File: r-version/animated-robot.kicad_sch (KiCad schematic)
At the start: 4 parts, among them J1 USB_C_Receptacle_USB2.0_16P, J2 Conn_02x03_Odd_Even, U1 LKS32MC034DOFxQx

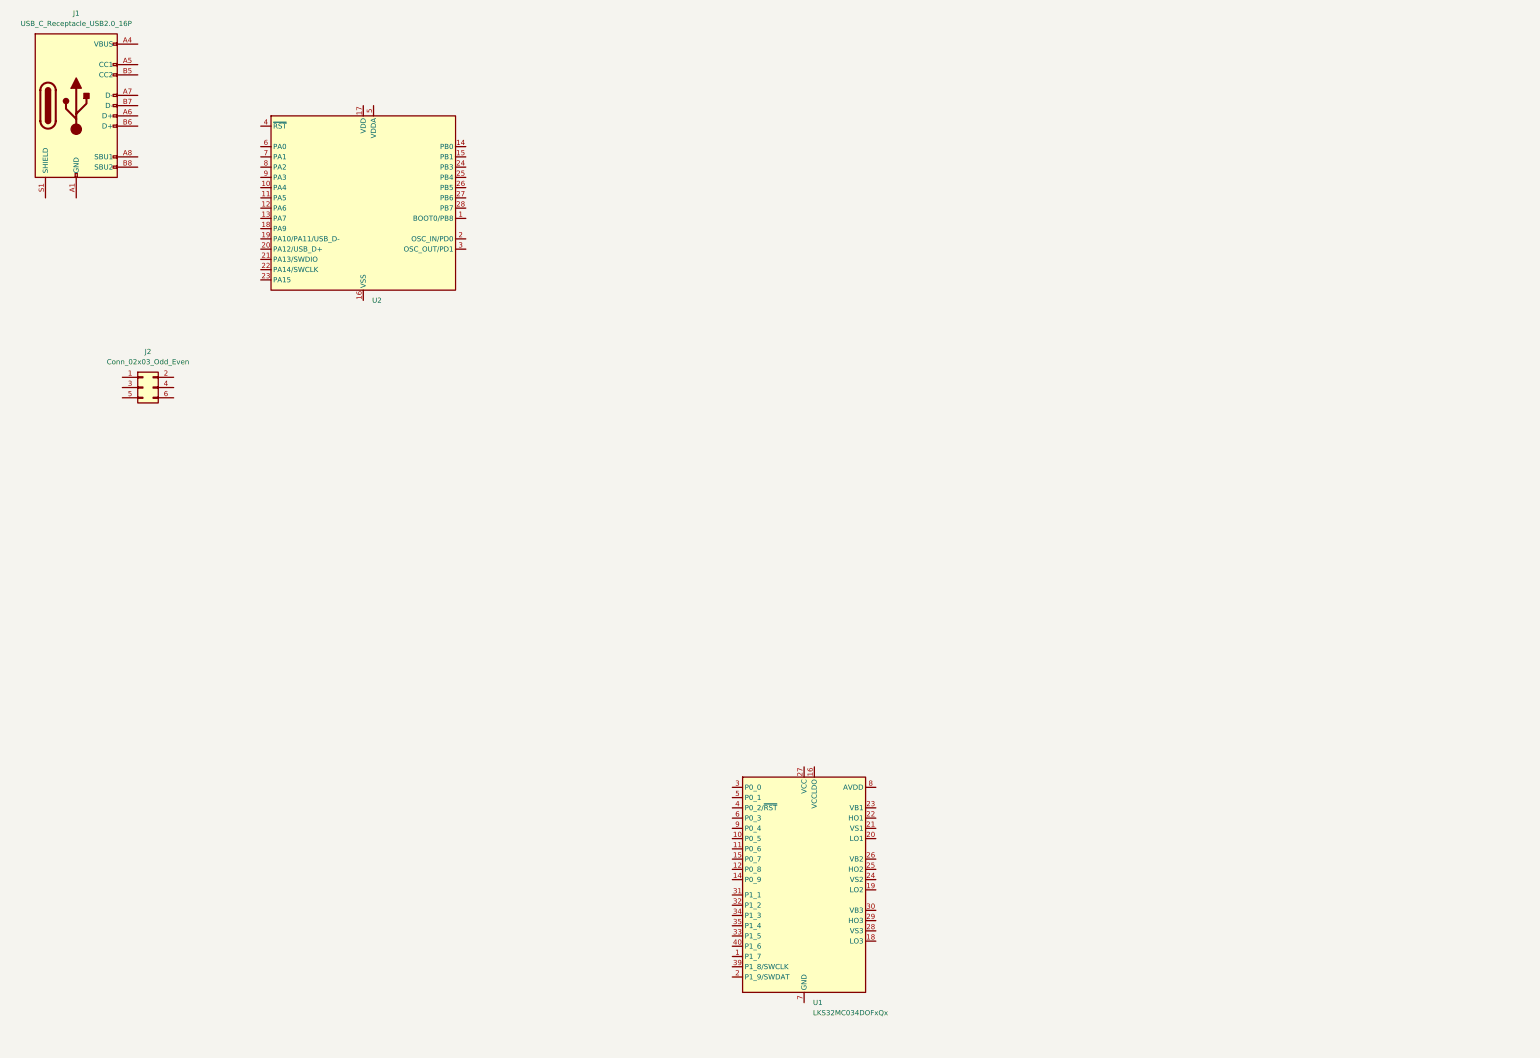
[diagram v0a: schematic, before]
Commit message: wch usb bridge section
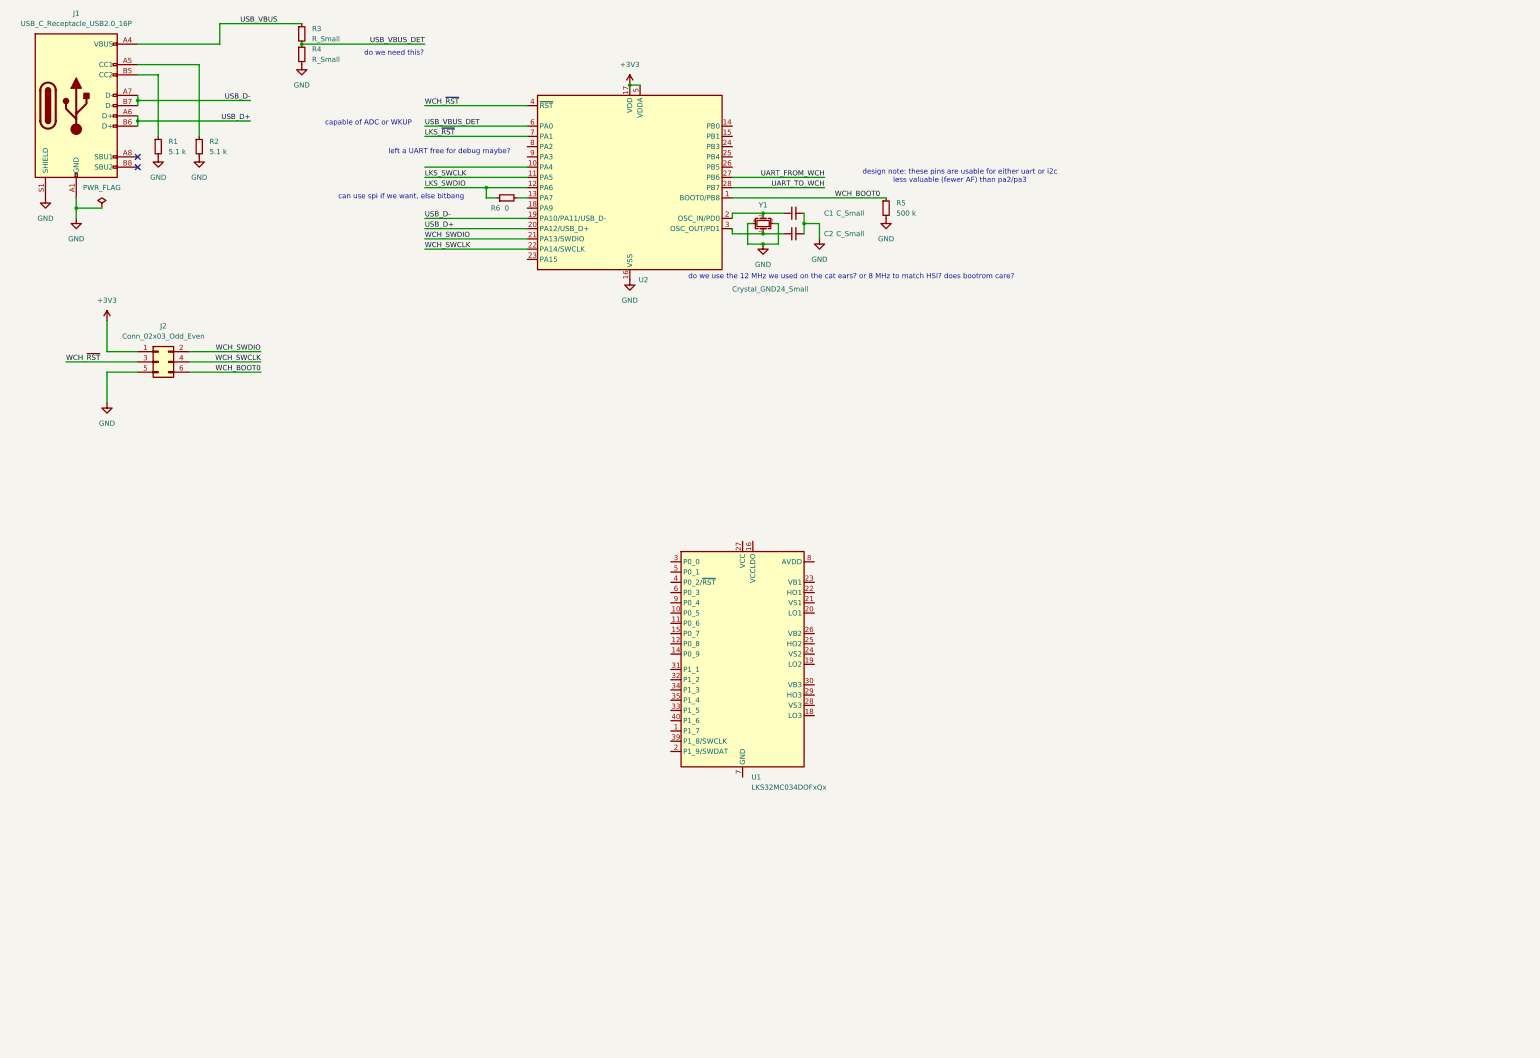
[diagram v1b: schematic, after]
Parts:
- removed U2: ~, symbol custom_parts:CH32V203GxRx
- added C1, C2: C_Small, symbol Device:C_Small
- added R1, R2: 5.1 k, symbol Device:R_Small
- added R3, R4: R_Small, symbol Device:R_Small
- added R5: 500 k, symbol Device:R_Small
- added R6: 0, symbol Device:R_Small
- added U2: ~, symbol custom_parts:CH32V203GxUx
- added Y1: Crystal_GND24_Small, symbol Device:Crystal_GND24_Small
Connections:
- net GND: now reaches J1.A1 (GND), J1.A12 (GND), J1.B1 (GND), J1.B12 (GND)
- net GND: now also J1.S1 (SHIELD), J2.5 (Pin_5), C1.2, C2.2, R1.2, R2.2, R4.2, R5.2, U2.16 (VSS), U2.29 (VSS), Y1.2, Y1.4
- net USB_VBUS: now reaches J1.A4 (VBUS), J1.A9 (VBUS), J1.B4 (VBUS), J1.B9 (VBUS)
- net USB_VBUS: now also R3.1
- net at J1.A5 (CC1): now also R2.1
- net USB_D+: now reaches J1.A6 (D+)
- net USB_D+: now also J1.B6 (D+), U2.20 (PA12/USB_D+)
- net USB_D-: now reaches J1.A7 (D-)
- net USB_D-: now also J1.B7 (D-), U2.19 (PA10/PA11/USB_D-)
- net at J1.B5 (CC2): now also R1.1
- net +3V3: now reaches J2.1 (Pin_1)
- net +3V3: now also U2.17 (VDD), U2.5 (VDDA)
- net WCH_SWDIO: now reaches J2.2 (Pin_2)
- net WCH_SWDIO: now also U2.21 (PA13/SWDIO)
- net WCH_~{RST}: now reaches J2.3 (Pin_3)
- net WCH_~{RST}: now also U2.4 (~{RST})
- net WCH_SWCLK: now reaches J2.4 (Pin_4)
- net WCH_SWCLK: now also U2.22 (PA14/SWCLK)
- net WCH_BOOT0: now reaches J2.6 (Pin_6)
- net WCH_BOOT0: now also R5.1, U2.1 (BOOT0/PB8)
- new net: C1.1, U2.2 (OSC_IN/PD0), Y1.3
- new net: R6.2, U2.13 (PA7)
- new net: C2.1, U2.3 (OSC_OUT/PD1), Y1.1
- new net LKS_SWCLK: U2.11 (PA5)
- new net LKS_SWDIO: R6.1, U2.12 (PA6)
- new net LKS_~{RST}: U2.7 (PA1)
- new net UART_FROM_WCH: U2.27 (PB6)
- new net UART_TO_WCH: U2.28 (PB7)
- new net USB_VBUS_DET: R3.2, R4.1, U2.6 (PA0)
- no-connect marks 0 -> 2
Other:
- note added: "can use spi if we want, else bitbang"
- note added: "capable of ADC or WKUP"
- note added: "design note: these pins are usable for either uart or i2c less valuable (fewer AF) than pa2/pa3"
- note added: "do we need this?"
- note added: "do we use the 12 MHz we used on the cat ears? or 8 MHz to match HSI? does bootrom care?"
- note added: "left a UART free for debug maybe?"
- moved on the sheet: J2, U1

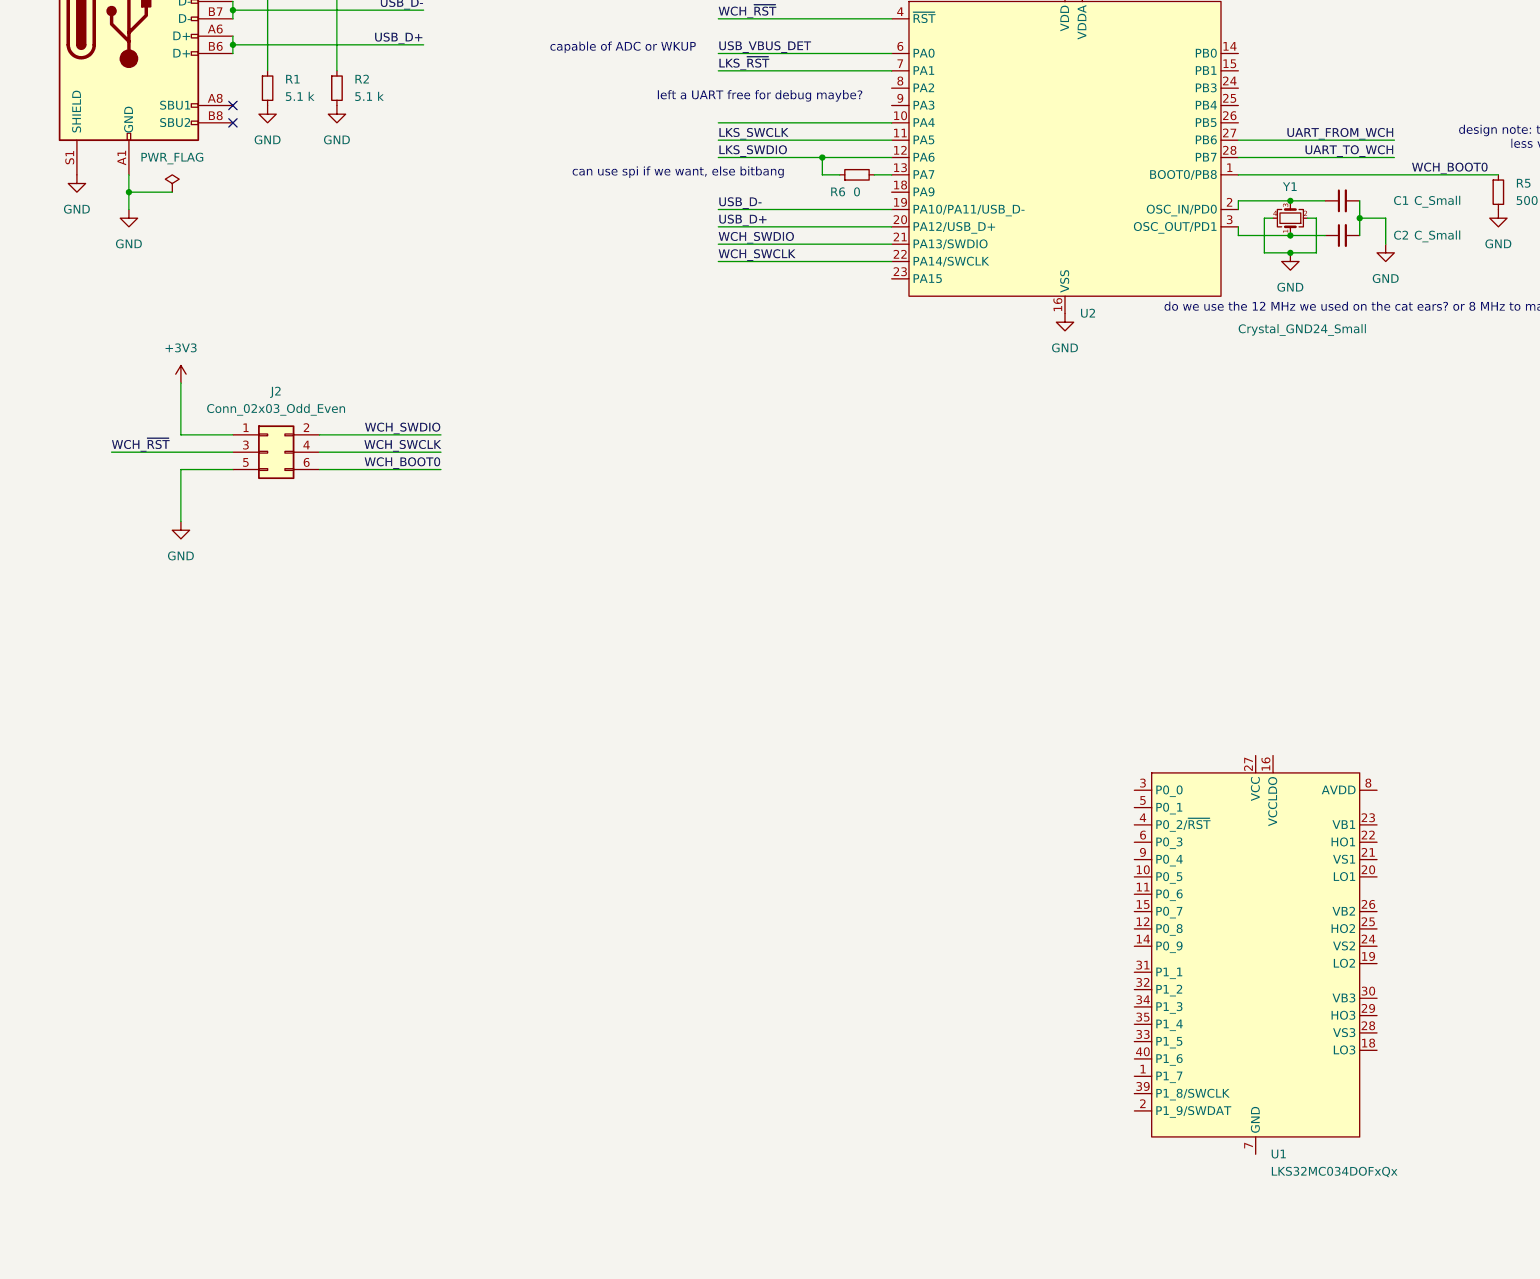
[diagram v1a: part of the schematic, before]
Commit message: lks32 digital section
also realize we don't want LDO version
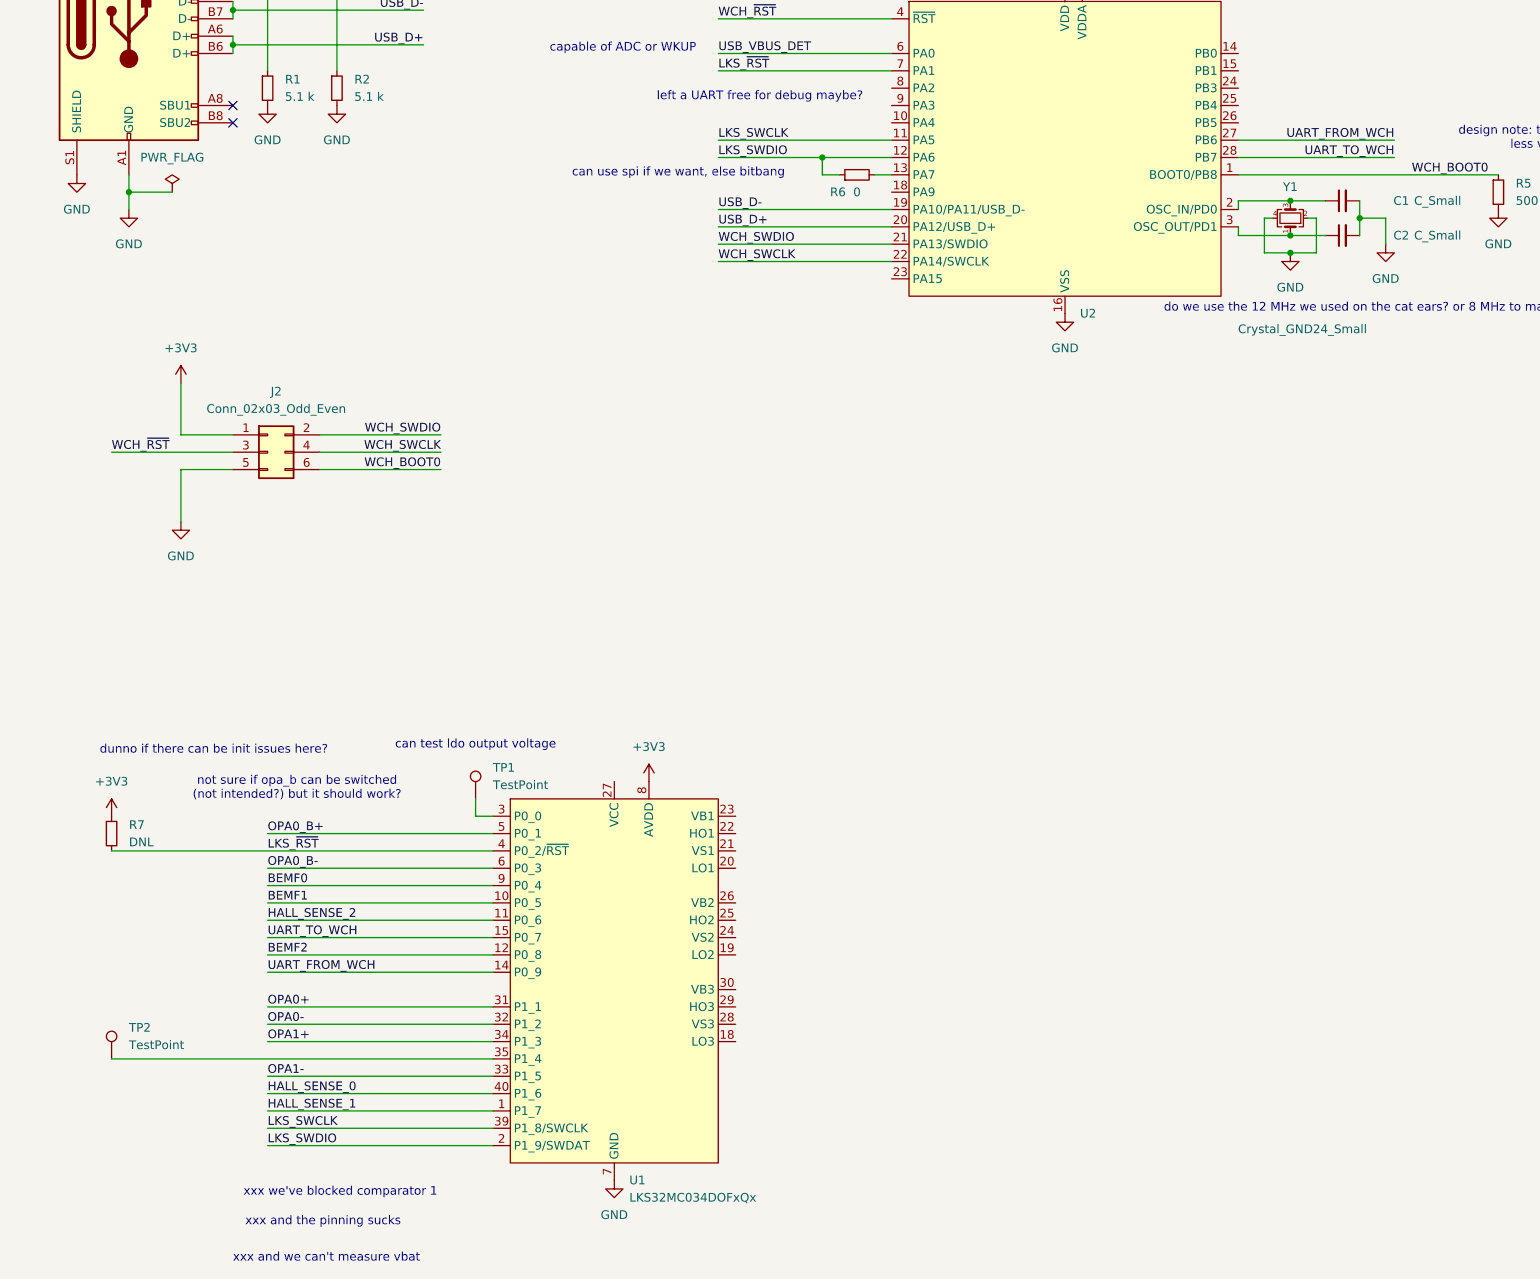
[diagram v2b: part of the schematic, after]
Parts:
- removed U1: LKS32MC034DOFxQx, Package_DFN_QFN:QFN-40-1EP_5x5mm_P0.4mm_EP3.6x3.6mm, symbol custom_parts:LKS32MC034DOFxQx
- added R7: DNL, symbol Device:R_Small
- added TP1, TP2: TestPoint, symbol Connector:TestPoint
- added U1: LKS32MC034DOFxQx, Package_DFN_QFN:QFN-40-1EP_5x5mm_P0.4mm_EP3.6x3.6mm, symbol custom_parts:LKS32MC034DFxQx
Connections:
- net +3V3: now also R7.1, U1.8 (AVDD)
- net GND: now also U1.13 (GND), U1.17 (GND), U1.41 (GND), U1.7 (GND)
- net LKS_SWCLK: now also U1.39 (P1_8/SWCLK)
- net LKS_SWDIO: now also U1.2 (P1_9/SWDAT)
- net LKS_~{RST}: now also R7.2, U1.4 (P0_2/~{RST})
- net UART_FROM_WCH: now also U1.14 (P0_9)
- net UART_TO_WCH: now also U1.15 (P0_7)
- new net: TP1.1, U1.3 (P0_0)
- new net: TP2.1, U1.35 (P1_4)
- new net BEMF0: U1.9 (P0_4)
- new net BEMF1: U1.10 (P0_5)
- new net BEMF2: U1.12 (P0_8)
- new net HALL_SENSE_0: U1.40 (P1_6)
- new net HALL_SENSE_1: U1.1 (P1_7)
- new net HALL_SENSE_2: U1.11 (P0_6)
- new net OPA0+: U1.31 (P1_1)
- new net OPA0-: U1.32 (P1_2)
- new net OPA0_B+: U1.5 (P0_1)
- new net OPA0_B-: U1.6 (P0_3)
- new net OPA1+: U1.34 (P1_3)
- new net OPA1-: U1.33 (P1_5)
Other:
- note added: "can test ldo output voltage"
- note added: "dunno if there can be init issues here?"
- note added: "not sure if opa_b can be switched (not intended?) but it should work?"
- note added: "xxx and the pinning sucks"
- note added: "xxx and we can't measure vbat"
- note added: "xxx we've blocked comparator 1"

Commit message: hbridge something like this?
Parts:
- added C10, C12, C14, C16, C4, C5, C6, C7: C_Small, symbol Device:C_Small
- added C11, C13, C15, C17, C8, C9: DNL, symbol Device:C_Small
- added C3: 0.1 uF, symbol Device:C_Small
- added D1: D_Schottky_Small, symbol Device:D_Schottky_Small
- added D10, D2, D3, D4, D5, D6, D7, D8, D9: D_Small, symbol Device:D_Small
- added J3: Conn_01x02, symbol Connector_Generic:Conn_01x02
- added L1: L, symbol Device:L
- added Q1, Q2, Q3, Q4, Q5, Q6: Q_NMOS_GDS, symbol Device:Q_NMOS_GDS
- added R10, R12, R13, R14, R15, R16, R18, R19, R20, R21, R24, R25, R26, R27, R29, R30, R31, R32, R33, R34: R_Small, symbol Device:R_Small
- added R11, R22, R28, R8: 5 m, symbol Device:R_Small
- added R17, R23, R9: 4.7, symbol Device:R_Small
- added U3: XL1509-ADJ, Package_SO:SOIC-8_3.9x4.9mm_P1.27mm, symbol Regulator_Switching:XL1509-ADJ
- R7: value DNL -> 10 k
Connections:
- net OPA0_B- is gone; now on net GNDPWR: U1.6 (P0_3)
- net OPA1- is gone; now on net GNDPWR: U1.33 (P1_5)
- net +3V3: now also C5.1, L1.2, R12.1
- net BEMF0: now also R29.2, R30.1
- net BEMF1: now also R31.2, R32.1
- net BEMF2: now also R33.2, R34.1
- net GND: now also C10.2, C14.2, C3.2, C4.2, C5.2, C6.2, D1.2 (A), J3.2 (Pin_2), R11.1, R13.2, R30.2, R32.2, R34.2, U3.4 (~{EN}), U3.5 (GND), U3.6 (GND), U3.7 (GND), U3.8 (GND)
- net LKS_~{RST}: now also C3.1
- net OPA0+: now also Q2.3 (S), R8.1
- net OPA0_B+: now also Q6.3 (S), R28.1
- net OPA1+: now also Q4.3 (S), R22.1
- net LO3: now reaches U1.18 (LO3)
- net LO3: now also D10.1 (K), R27.1
- net LO2: now reaches U1.19 (LO2)
- net LO2: now also D7.1 (K), R21.1
- net LO1: now reaches U1.20 (LO1)
- net LO1: now also D4.1 (K), R16.1
- net MOT1: now reaches U1.21 (VS1)
- net MOT1: now also C7.2, C8.2, Q1.3 (S), Q2.2 (D), R29.1
- net HO1: now reaches U1.22 (HO1)
- net HO1: now also D3.1 (K), R14.1
- net VB1: now reaches U1.23 (VB1)
- net VB1: now also C7.1, R9.2
- net MOT2: now reaches U1.24 (VS2)
- net MOT2: now also C11.2, C12.2, Q3.3 (S), Q4.2 (D), R31.1
- net HO2: now reaches U1.25 (HO2)
- net HO2: now also D6.1 (K), R19.1
- net VB2: now reaches U1.26 (VB2)
- net VB2: now also C12.1, R17.2
- net +BATT: now reaches U1.27 (VCC)
- net +BATT: now also C10.1, C14.1, C4.1, C6.1, D2.2 (A), D5.2 (A), D8.2 (A), J3.1 (Pin_1), Q1.2 (D), Q3.2 (D), Q5.2 (D), U3.1 (VIN)
- net MOT3: now reaches U1.28 (VS3)
- net MOT3: now also C15.2, C16.2, Q5.3 (S), Q6.2 (D), R33.1
- net HO3: now reaches U1.29 (HO3)
- net HO3: now also D9.1 (K), R25.1
- net VB3: now reaches U1.30 (VB3)
- net VB3: now also C16.1, R23.2
- net OPA0- renamed GNDPWR
- net GNDPWR: now also C13.2, C17.2, C9.2, R11.2, R22.2, R28.2, R8.2
- new net: D6.2 (A), R18.1
- new net: C11.1, Q3.1 (G), R18.2, R19.2
- new net: D7.2 (A), R20.1
- new net: C13.1, Q4.1 (G), R20.2, R21.2
- new net: D9.2 (A), R24.1
- new net: C9.1, Q2.1 (G), R15.2, R16.2
- new net: D4.2 (A), R15.1
- new net: C17.1, Q6.1 (G), R26.2, R27.2
- new net: C8.1, Q1.1 (G), R10.2, R14.2
- new net: D10.2 (A), R26.1
- new net: C15.1, Q5.1 (G), R24.2, R25.2
- new net: D2.1 (K), R9.1
- new net: D8.1 (K), R23.1
- new net: D1.1 (K), L1.1, U3.2 (OUT)
- new net: R12.2, R13.1, U3.3 (FB)
- new net: D5.1 (K), R17.1
- new net: D3.2 (A), R10.1
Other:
- note added: "hard limit 20v --> 4s?"
- note added: "xxx todo"
- note removed: "dunno if there can be init issues here?"

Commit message: have a poke
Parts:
- removed TP1: TestPoint, symbol Connector:TestPoint
- added J4: Conn_01x05, symbol Connector_Generic:Conn_01x05
- added R35, R36: R_Small, symbol Device:R_Small
- added TP3, TP4: TestPoint, symbol Connector:TestPoint
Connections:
- net +3V3: now also J4.1 (Pin_1)
- net +BATT: now also R35.1
- net GND: now also J4.5 (Pin_5), R36.2
- net HALL_SENSE_0: now also J4.2 (Pin_2)
- net HALL_SENSE_1: now also J4.3 (Pin_3)
- net HALL_SENSE_2: now also J4.4 (Pin_4)
- net at U2.8 (PA2): now also TP3.1
- net at U2.9 (PA3): now also TP4.1
- net VBAT_MEAS: now reaches U1.3 (P0_0)
- net VBAT_MEAS: now also R35.2, R36.1
- no-connect marks 2 -> 10
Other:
- note added: "xxx can we reliably do e-stop with this?"
- note removed: "can test ldo output voltage"
- note removed: "xxx and we can't measure vbat"
- moved on the sheet: C12, C16, C7
